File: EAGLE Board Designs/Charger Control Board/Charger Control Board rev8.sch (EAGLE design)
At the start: 114 parts, among them K1 RELAY_DPDT, K2 RELAY_DPDT, K3 RELAY_DPDT, U1 LOGICGATE_BUFFER, U100 MCP2562FD, U101 MCP2562FD, U2 ADM8316WBX30, U3 VOLTAGE_REGULATOR_MODULE_OKI-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

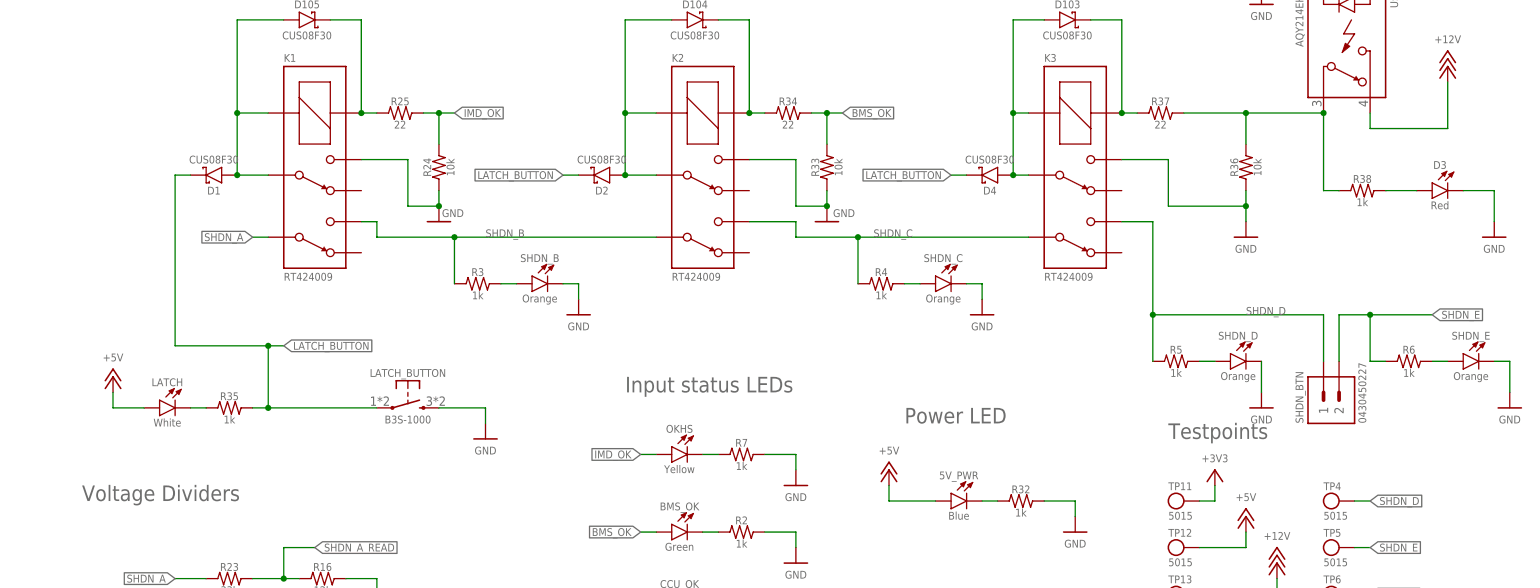
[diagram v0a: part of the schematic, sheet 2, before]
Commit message: Schematic changes
- Fixed r100 value
- Added latch led pulldown
- Changed 2 pin connectors to horizontal
- Removed second software shdn led
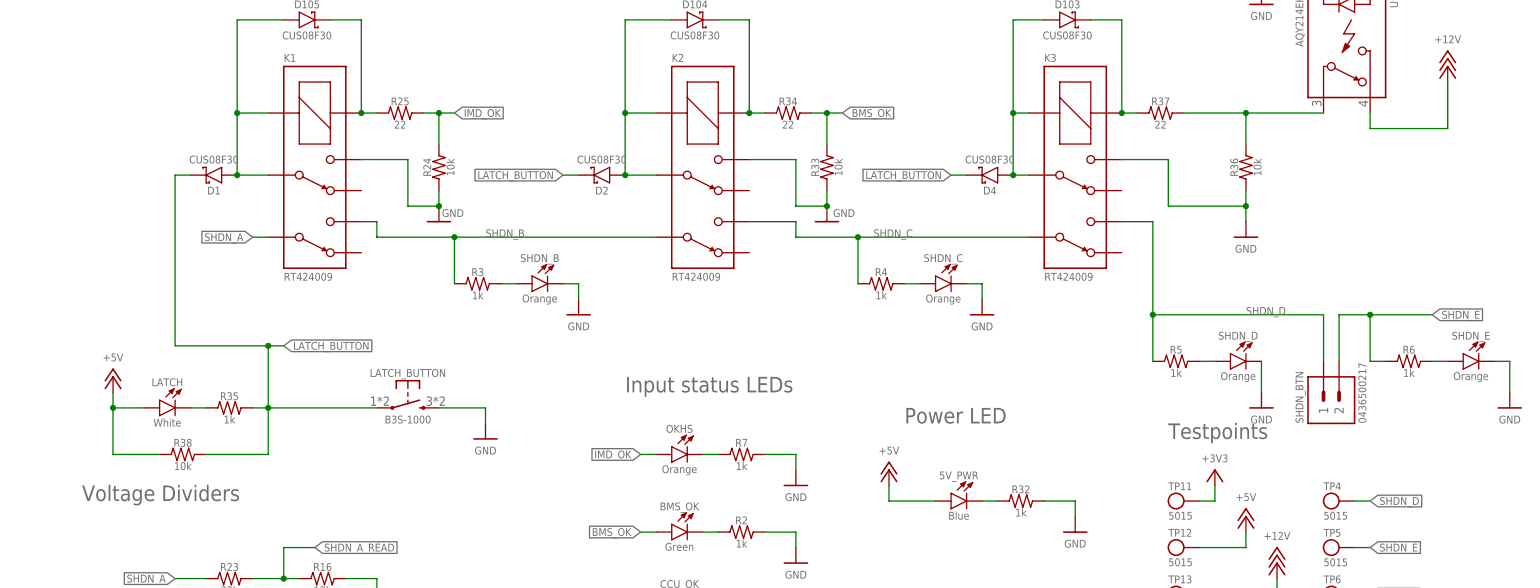
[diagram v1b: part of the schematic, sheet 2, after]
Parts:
- removed D3: LED_0603_RED, HyTechDevices:LED_0603_RED
- OKHS: value LED_0603_YELLOW -> LED_0603_ORANGE; device HyTechDevices:LED_0603_YELLOW -> HyTechDevices:LED_0603_ORANGE
- POWER, SHDN_BTN: value CONNECTOR-2_μF_T_V_ -> CONNECTOR-2_MF_T_V_; device HyTechDevices:CONNECTOR-2_μF_T_V_ -> HyTechDevices:CONNECTOR-2_MF_T_V_BLACK
- R100: value RESISTOR_0603_240 -> RESISTOR_0603_1.33K; device HyTechDevices_Jumper:RESISTOR_0603_240 -> HyTechDevices:RESISTOR_0603_1.33K
- R38: value RESISTOR_0603_1K -> RESISTOR_0603_10K; device HyTechDevices:RESISTOR_0603_1K -> HyTechDevices:RESISTOR_0603_10K
- U$100, U$4: device HyTechDevices:RELAY_SOLIDSTATE_NO -> HyTechDevices_temp:RELAY_SOLIDSTATE_NO
- U2: device HyTechDevices:ADM8316WBX30 -> HyTechDevices_temp:ADM8316WBX30
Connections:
- removed net N$21: D3.A, R38.2
- net +5V: now also R38.1
- net GND: no longer D3.C
- net LATCH_BUTTON: now also R38.2
- net N$16: no longer R38.1
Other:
- moved on the sheet: R38
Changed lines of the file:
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@@
 <part name="R37" library="HyTechDevices" deviceset="RESISTOR_?_*" device="0603" technology="22"/>
 <part name="R25" library="HyTechDevices" deviceset="RESISTOR_?_*" device="0603" technology="22"/>
-<part name="R38" library="HyTechDevices" deviceset="RESISTOR_?_*" device="0603" technology="1K"/>
-<part name="D3" library="HyTechDevices" deviceset="LED_?_*" device="0603" technology="RED"/>
-<part name="P32" library="HyTechSupplies" deviceset="GND" device=""/>
 <part name="R36" library="HyTechDevices" deviceset="RESISTOR_?_*" device="0603" technology="10K"/>
 <part name="P33" library="HyTechSupplies" deviceset="GND" device=""/>
@@
 <part name="R32" library="HyTechDevices" deviceset="RESISTOR_?_*" device="0603" technology="1K"/>
 <part name="P54" library="HyTechSupplies" deviceset="GND" device=""/>
-<part name="OKHS" library="HyTechDevices" deviceset="LED_?_*" device="0603" technology="YELLOW"/>
+<part name="OKHS" library="HyTechDevices" deviceset="LED_?_*" device="0603" technology="ORANGE" value="LED_0603_ORANGE"/>
 <part name="BMS_OK" library="HyTechDevices" deviceset="LED_?_*" device="0603" technology="GREEN"/>
 <part name="STATUS_4.0" library="HyTechDevices" deviceset="LED_?_*" device="0603" technology="RED"/>
@@
 <part name="P57" library="HyTechSupplies" deviceset="+12V" device=""/>
 <part name="P58" library="HyTechSupplies" deviceset="GND" device=""/>
-<part name="POWER" library="HyTechDevices" deviceset="CONNECTOR-2_?_*" device="μF_T_V" value="CONNECTOR-2_μF_T_V_"/>
-<part name="SHDN_BTN" library="HyTechDevices" deviceset="CONNECTOR-2_?_*" device="μF_T_V" value="CONNECTOR-2_μF_T_V_"/>
-<part name="U2" library="HyTechDevices" deviceset="ADM8316" device="" technology="WBX30" value="ADM8316WBX30"/>
+<part name="POWER" library="HyTechDevices" deviceset="CONNECTOR-2_?_*" device="MF_T_V" technology="BLACK" value="CONNECTOR-2_MF_T_V_"/>
+<part name="SHDN_BTN" library="HyTechDevices" deviceset="CONNECTOR-2_?_*" device="MF_T_V" technology="BLACK" value="CONNECTOR-2_MF_T_V_"/>
+<part name="U2" library="HyTechDevices_temp" deviceset="ADM8316" device="" technology="WBX30" value="ADM8316WBX30"/>
 <part name="R28" library="HyTechDevices" deviceset="RESISTOR_?_*" device="0603" technology="10K"/>
 <part name="R29" library="HyTechDevices" deviceset="RESISTOR_?_*" device="0603" technology="10K" value="RESISTOR_0603_10K"/>
@@
 <attribute name="SIGNAL" value="SHDN_F"/>
 </part>
-<part name="U$4" library="HyTechDevices" deviceset="RELAY_SOLIDSTATE_NO" device=""/>
+<part name="U$4" library="HyTechDevices_temp" deviceset="RELAY_SOLIDSTATE_NO" device=""/>
 <part name="4.1_ONLY" library="HyTechDevices_Jumper" deviceset="JUMPER_?_*" device="" technology="1X02"/>
 <part name="CAN_TERM" library="HyTechDevices_Jumper" deviceset="JUMPER_?_*" device="" technology="1X02"/>
@@
 <part name="SHDN_F" library="HyTechDevices" deviceset="LED_?_*" device="0603" technology="ORANGE"/>
 <part name="CCU_OK" library="HyTechDevices" deviceset="LED_?_*" device="0603" technology="GREEN"/>
-<part name="U$100" library="HyTechDevices" deviceset="RELAY_SOLIDSTATE_NO" device=""/>
+<part name="U$100" library="HyTechDevices_temp" deviceset="RELAY_SOLIDSTATE_NO" device=""/>
 <part name="E_SELECT" library="HyTechDevices_Jumper" deviceset="JUMPER_?_*" device="0603" value="JUMPER_0603_"/>
 <part name="F_SELECT" library="HyTechDevices_Jumper" deviceset="JUMPER_?_*" device="0603" value="JUMPER_0603_"/>
-<part name="R100" library="HyTechDevices_Jumper" deviceset="RESISTOR_?_*" device="0603" technology="240"/>
+<part name="R100" library="HyTechDevices" deviceset="RESISTOR_?_*" device="0603" technology="1.33K" value="RESISTOR_0603_1.33K"/>
 <part name="P67" library="HyTechSupplies" deviceset="GND" device=""/>
 <part name="P68" library="HyTechSupplies" deviceset="GND" device=""/>
@@
 <part name="XB1" library="HyTechDevices" deviceset="BATTERY_HOLDER_*" device="KEYSTONE_498"/>
 <part name="U3" library="HyTechDevices" deviceset="VOLTAGE_REGULATOR_MODULE_?_*" device="OKI-78SR" technology="5V"/>
+<part name="R38" library="HyTechDevices" deviceset="RESISTOR_?_*" device="0603" technology="10K"/>
 </parts>
 <sheets>
@@
 <attribute name="RESISTANCE" x="69.85" y="179.07" size="1.27" layer="96" align="top-center"/>
 </instance>
-<instance part="R38" gate="G$1" x="228.6" y="167.64" smashed="yes">
-<attribute name="NAME" x="227.33" y="168.91" size="1.27" layer="95" align="bottom-center"/>
-<attribute name="RESISTANCE" x="227.33" y="166.37" size="1.27" layer="96" align="top-center"/>
-</instance>
-<instance part="D3" gate="LED" x="241.3" y="167.64" smashed="yes">
-<attribute name="COLOR" x="240.03" y="165.862" size="1.27" layer="95" align="top-center"/>
-<attribute name="NAME" x="240.03" y="171.196" size="1.27" layer="96" align="bottom-center"/>
-</instance>
-<instance part="P32" gate="1" x="248.92" y="160.02" smashed="yes">
-<attribute name="VALUE" x="248.92" y="158.75" size="1.27" layer="96" align="top-center"/>
-</instance>
 <instance part="R36" gate="G$1" x="208.28" y="172.72" smashed="yes" rot="R90">
 <attribute name="NAME" x="207.01" y="171.45" size="1.27" layer="95" rot="R90" align="bottom-center"/>
@@
 <attribute name="COLOR" x="115.57" y="97.282" size="1.27" layer="95" align="top-center"/>
 <attribute name="NAME" x="115.57" y="102.616" size="1.27" layer="96" align="bottom-center"/>
+</instance>
+<instance part="R38" gate="G$1" x="35.56" y="124.46" smashed="yes">
+<attribute name="NAME" x="34.29" y="125.73" size="1.27" layer="95" align="bottom-center"/>
+<attribute name="RESISTANCE" x="34.29" y="123.19" size="1.27" layer="96" align="top-center"/>
 </instance>
 </instances>
@@
 <pinref part="P30" gate="1" pin="GND"/>
 <pinref part="U$4" gate="G$1" pin="CONTROL-"/>
-</segment>
-<segment>
-<pinref part="D3" gate="LED" pin="C"/>
-<wire x1="243.84" y1="167.64" x2="248.92" y2="167.64" width="0.1524" layer="91"/>
-<pinref part="P32" gate="1" pin="GND"/>
-<wire x1="248.92" y1="167.64" x2="248.92" y2="162.56" width="0.1524" layer="91"/>
 </segment>
 <segment>
@@
 <wire x1="220.98" y1="180.34" x2="208.28" y2="180.34" width="0.1524" layer="91"/>
 <wire x1="208.28" y1="180.34" x2="198.12" y2="180.34" width="0.1524" layer="91"/>
-<wire x1="220.98" y1="180.34" x2="220.98" y2="167.64" width="0.1524" layer="91"/>
-<pinref part="R38" gate="G$1" pin="1"/>
-<wire x1="220.98" y1="167.64" x2="223.52" y2="167.64" width="0.1524" layer="91"/>
 <pinref part="R36" gate="G$1" pin="2"/>
 <wire x1="208.28" y1="175.26" x2="208.28" y2="180.34" width="0.1524" layer="91"/>
 <junction x="208.28" y="180.34"/>
 <pinref part="U$4" gate="G$1" pin="CONTACT1"/>
-<junction x="220.98" y="180.34"/>
 </segment>
 </net>
@@
 <pinref part="D4" gate="G$1" pin="A"/>
 <junction x="170.18" y="170.18"/>
-</segment>
-</net>
-<net name="N$21" class="0">
-<segment>
-<pinref part="R38" gate="G$1" pin="2"/>
-<pinref part="D3" gate="LED" pin="A"/>
-<wire x1="231.14" y1="167.64" x2="236.22" y2="167.64" width="0.1524" layer="91"/>
 </segment>
 </net>
@@
 <pinref part="D1" gate="G$1" pin="C"/>
 <pinref part="LATCH_BUTTON" gate="G$1" pin="P"/>
+<pinref part="R38" gate="G$1" pin="2"/>
+<wire x1="38.1" y1="124.46" x2="48.26" y2="124.46" width="0.1524" layer="91"/>
+<wire x1="48.26" y1="124.46" x2="48.26" y2="132.08" width="0.1524" layer="91"/>
 </segment>
 <segment>
@@
 <wire x1="22.86" y1="134.62" x2="22.86" y2="132.08" width="0.1524" layer="91"/>
 <wire x1="22.86" y1="132.08" x2="27.94" y2="132.08" width="0.1524" layer="91"/>
-</segment>
-<segment>
+<wire x1="22.86" y1="132.08" x2="22.86" y2="124.46" width="0.1524" layer="91"/>
+<junction x="22.86" y="132.08"/>
+<pinref part="R38" gate="G$1" pin="1"/>
+<wire x1="22.86" y1="124.46" x2="30.48" y2="124.46" width="0.1524" layer="91"/>
+</segment>
+<segment>

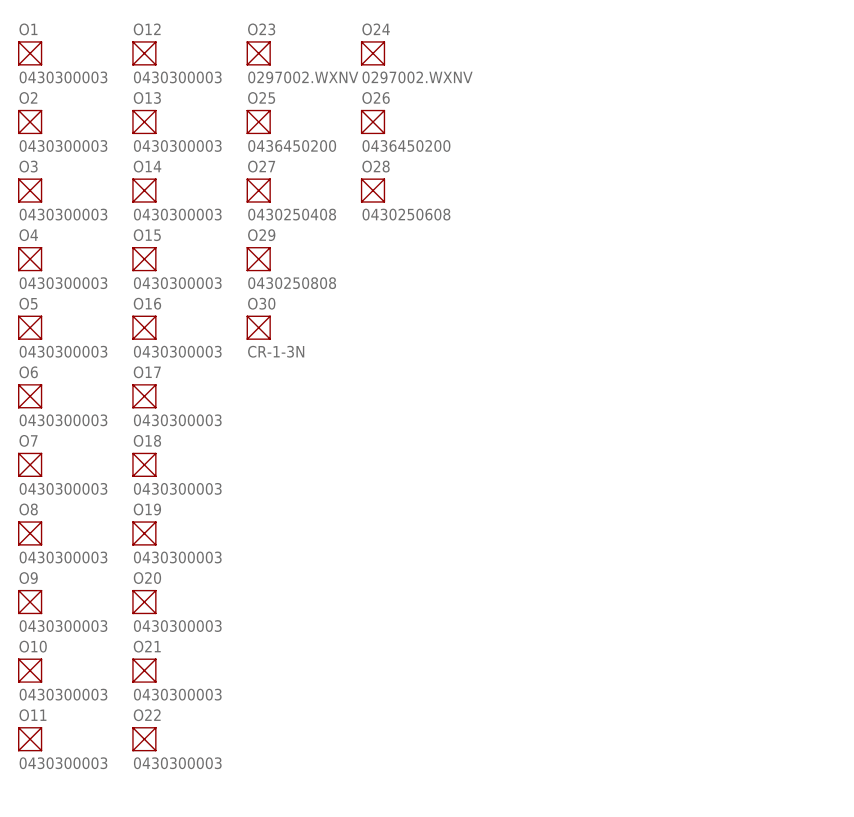
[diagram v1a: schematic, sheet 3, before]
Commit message: Cleaned up silkscreen
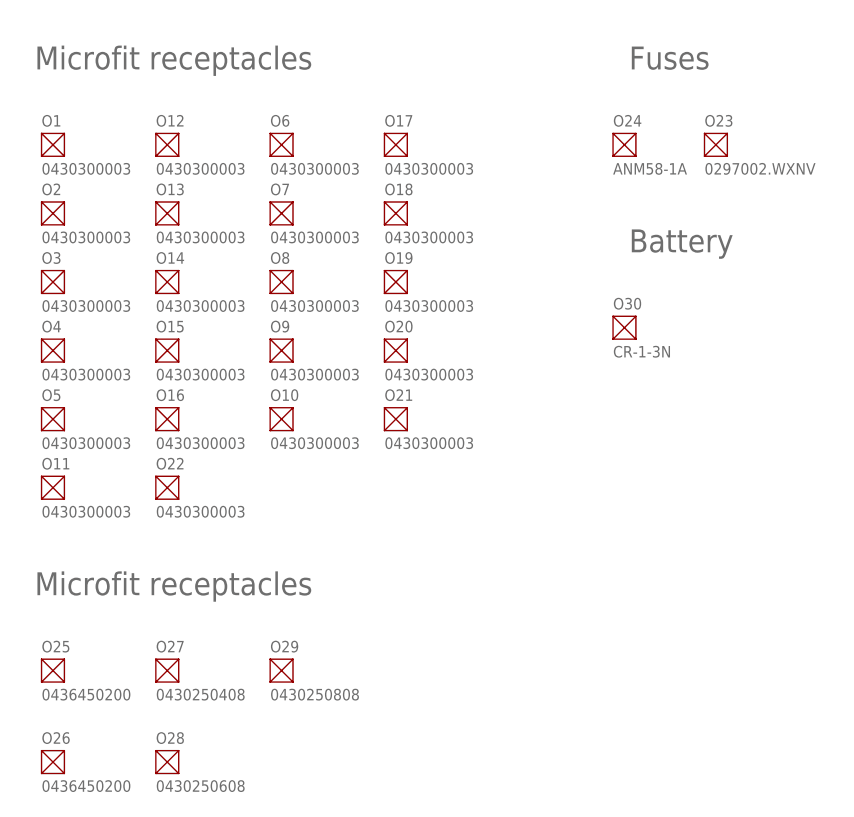
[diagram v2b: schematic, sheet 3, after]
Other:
- note added: "Battery"
- note added: "Fuses"
- note added: "Microfit receptacles"
- moved on the sheet: O1, O10, O11, O12, O13, O14, O15, O16, O17, O18, O19, O2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

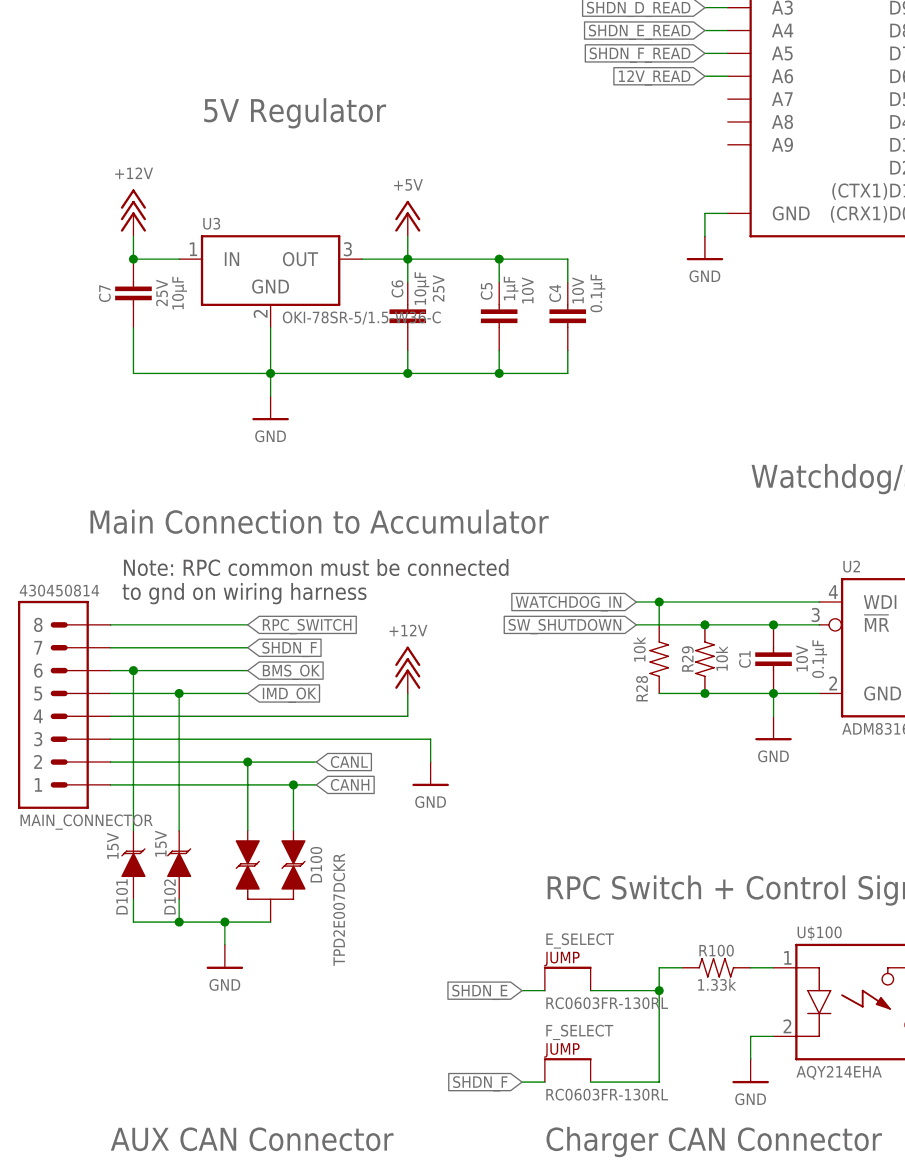
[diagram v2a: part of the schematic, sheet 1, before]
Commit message: Switched R100 to 1k, added input filtering to 5v regulator
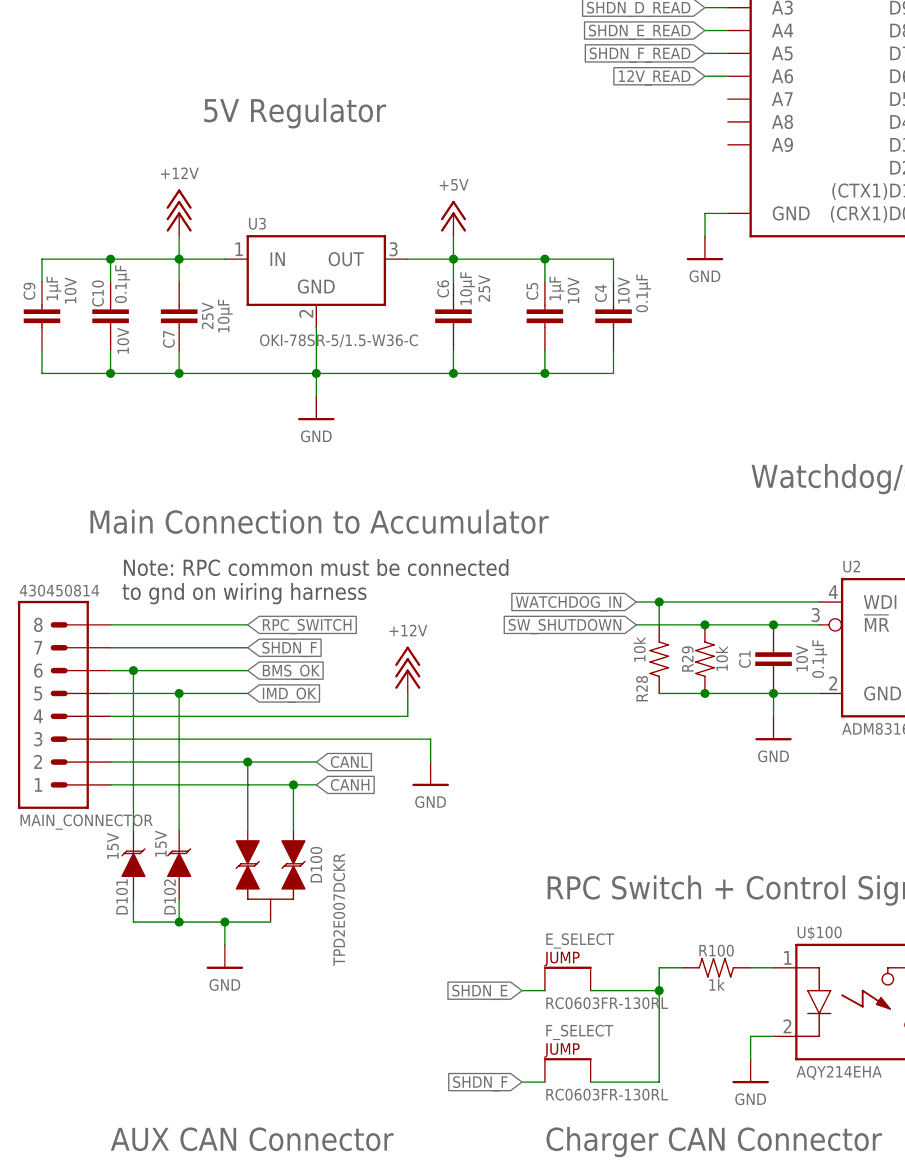
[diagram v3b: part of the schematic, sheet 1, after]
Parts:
- added C10: CAPACITOR_0603_10V_0.1UF, HyTechDevices:CAPACITOR_0603_10V_0.1UF
- added C9: CAPACITOR_0603_10V_1UF, HyTechDevices:CAPACITOR_0603_10V_1UF
- R100: value RESISTOR_0603_1.33K -> RESISTOR_0603_1K; device HyTechDevices:RESISTOR_0603_1.33K -> HyTechDevices:RESISTOR_0603_1K
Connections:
- net +12V: now also C10.2, C9.1
- net GND: now also C10.1, C9.2
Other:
- moved on the sheet: C4, C5, C6, C7, U3
